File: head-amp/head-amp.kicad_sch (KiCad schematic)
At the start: 32 parts, among them IC1 OPA1642AID

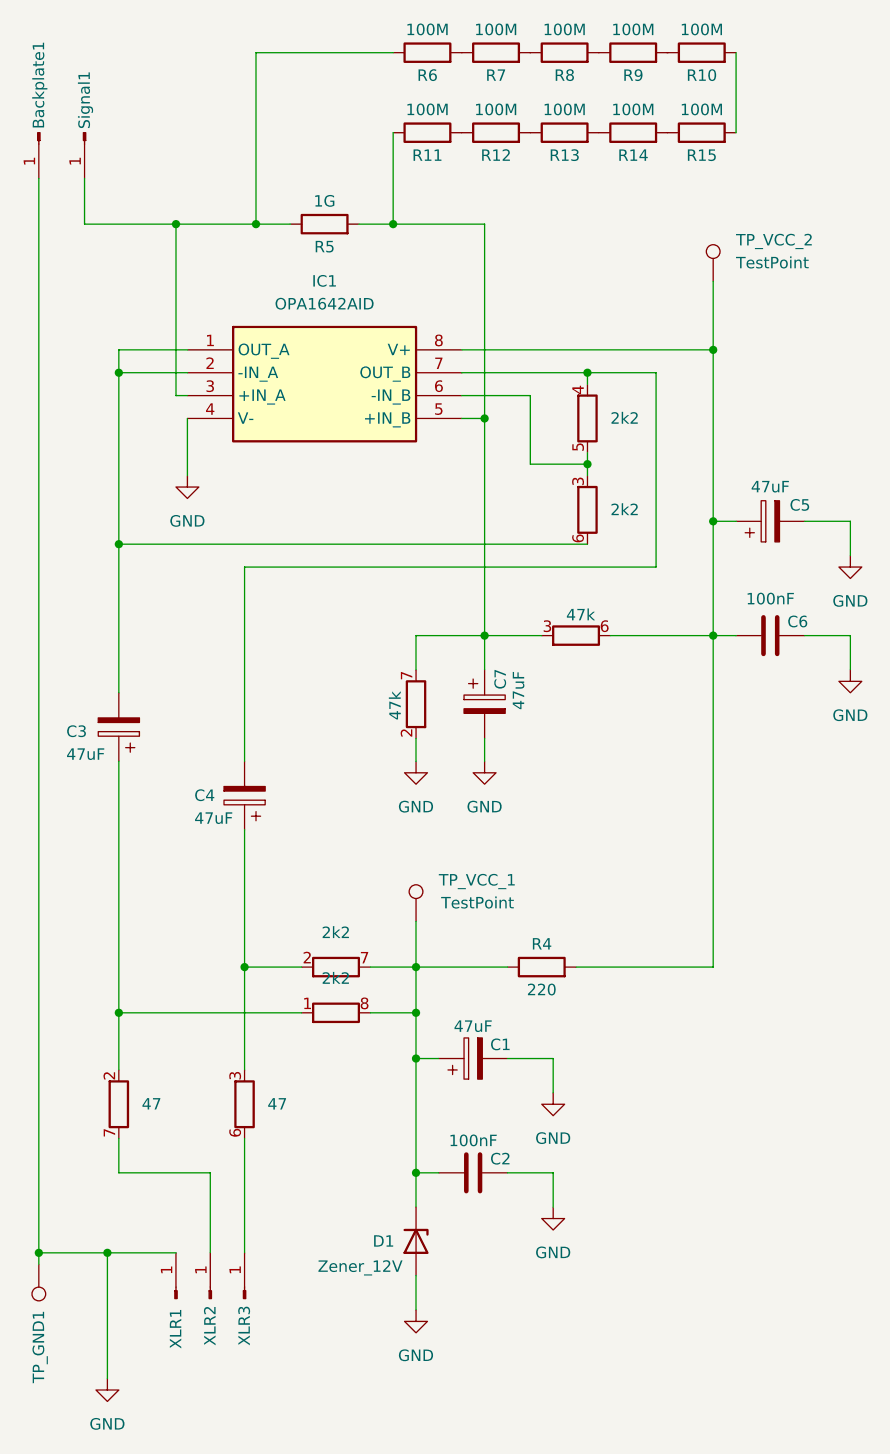
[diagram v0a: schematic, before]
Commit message: Finished head amp PCB layout, generated gerber + BOM
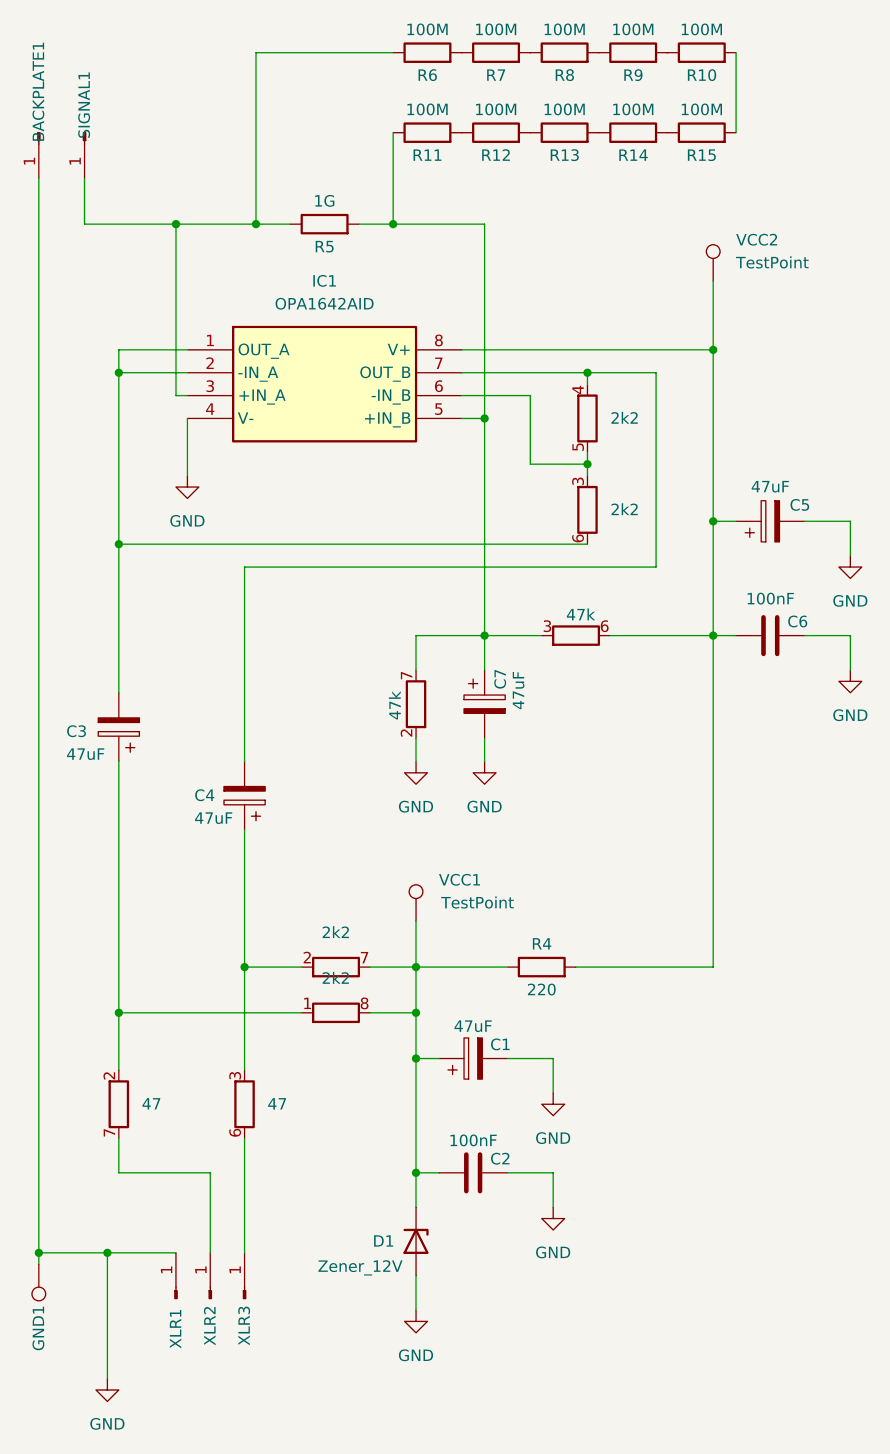
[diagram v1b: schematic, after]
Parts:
- BACKPLATE1: renamed from Backplate1; footprint Connector_Wire:SolderWire-0.1sqmm_1x01_D0.4mm_OD1mm -> Connector_Wire:SolderWire-0.25sqmm_1x01_D0.65mm_OD2mm
- SIGNAL1: renamed from Signal1; footprint Connector_Wire:SolderWire-0.1sqmm_1x01_D0.4mm_OD1mm -> Connector_Wire:SolderWire-0.25sqmm_1x01_D0.65mm_OD2mm
- XLR1, XLR2, XLR3: footprint Connector_Wire:SolderWire-0.1sqmm_1x01_D0.4mm_OD1mm -> Connector_Wire:SolderWire-0.25sqmm_1x01_D0.65mm_OD2mm
- renumbered TP_GND1 to GND1, TP_VCC_1 to VCC1, TP_VCC_2 to VCC2
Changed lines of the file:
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@@
 		(on_board yes)
 		(dnp no)
-		(property "Reference" "TP_GND1"
-			(at 43.18 178.308 90)
+		(property "Reference" "GND1"
+			(at 43.18 174.752 90)
 			(effects
 				(font
@@
 			(project "head-amp"
 				(path "/7025f093-8497-445c-bb21-7e3d97d178d1"
-					(reference "TP_GND1")
+					(reference "GND1")
 					(unit 1)
 				)
@@
 			)
 		)
-		(property "Footprint" "Connector_Wire:SolderWire-0.1sqmm_1x01_D0.4mm_OD1mm"
+		(property "Footprint" "Connector_Wire:SolderWire-0.25sqmm_1x01_D0.65mm_OD2mm"
 			(at 62.23 168.91 0)
 			(effects
@@
 		(on_board yes)
 		(dnp no)
-		(property "Reference" "Signal1"
+		(property "Reference" "SIGNAL1"
 			(at 48.26 32.512 0)
 			(effects
@@
 			)
 		)
-		(property "Footprint" "Connector_Wire:SolderWire-0.1sqmm_1x01_D0.4mm_OD1mm"
+		(property "Footprint" "Connector_Wire:SolderWire-0.25sqmm_1x01_D0.65mm_OD2mm"
 			(at 48.26 39.37 0)
 			(effects
@@
 			(project "head-amp"
 				(path "/7025f093-8497-445c-bb21-7e3d97d178d1"
-					(reference "Signal1")
+					(reference "SIGNAL1")
 					(unit 1)
 				)
@@
 		(dnp no)
 		(fields_autoplaced yes)
-		(property "Reference" "TP_VCC_2"
+		(property "Reference" "VCC2"
 			(at 120.65 51.3079 0)
 			(effects
@@
 			(project ""
 				(path "/7025f093-8497-445c-bb21-7e3d97d178d1"
-					(reference "TP_VCC_2")
+					(reference "VCC2")
 					(unit 1)
 				)
@@
 		(on_board yes)
 		(dnp no)
-		(property "Reference" "Backplate1"
+		(property "Reference" "BACKPLATE1"
 			(at 43.18 29.21 0)
 			(effects
@@
 			)
 		)
-		(property "Footprint" "Connector_Wire:SolderWire-0.1sqmm_1x01_D0.4mm_OD1mm"
+		(property "Footprint" "Connector_Wire:SolderWire-0.25sqmm_1x01_D0.65mm_OD2mm"
 			(at 43.18 39.37 0)
 			(effects
@@
 			)
 		)
-		(property "Datasheet" "~"
+		(property "Datasheet" ""
 			(at 43.18 39.37 0)
 			(effects
@@
 			(project ""
 				(path "/7025f093-8497-445c-bb21-7e3d97d178d1"
-					(reference "Backplate1")
+					(reference "BACKPLATE1")
 					(unit 1)
 				)
@@
 			)
 		)
-		(property "Footprint" "Connector_Wire:SolderWire-0.1sqmm_1x01_D0.4mm_OD1mm"
+		(property "Footprint" "Connector_Wire:SolderWire-0.25sqmm_1x01_D0.65mm_OD2mm"
 			(at 66.04 168.91 0)
 			(effects
@@
 		(on_board yes)
 		(dnp no)
-		(property "Reference" "TP_VCC_1"
+		(property "Reference" "VCC1"
 			(at 87.63 122.4279 0)
 			(effects
@@
 			(project "head-amp"
 				(path "/7025f093-8497-445c-bb21-7e3d97d178d1"
-					(reference "TP_VCC_1")
+					(reference "VCC1")
 					(unit 1)
 				)
@@
 			)
 		)
-		(property "Footprint" "Connector_Wire:SolderWire-0.1sqmm_1x01_D0.4mm_OD1mm"
+		(property "Footprint" "Connector_Wire:SolderWire-0.25sqmm_1x01_D0.65mm_OD2mm"
 			(at 58.42 168.91 0)
 			(effects

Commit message: input/output connectors moved to 2.54mm spacing. Improved clearance around screw slots.
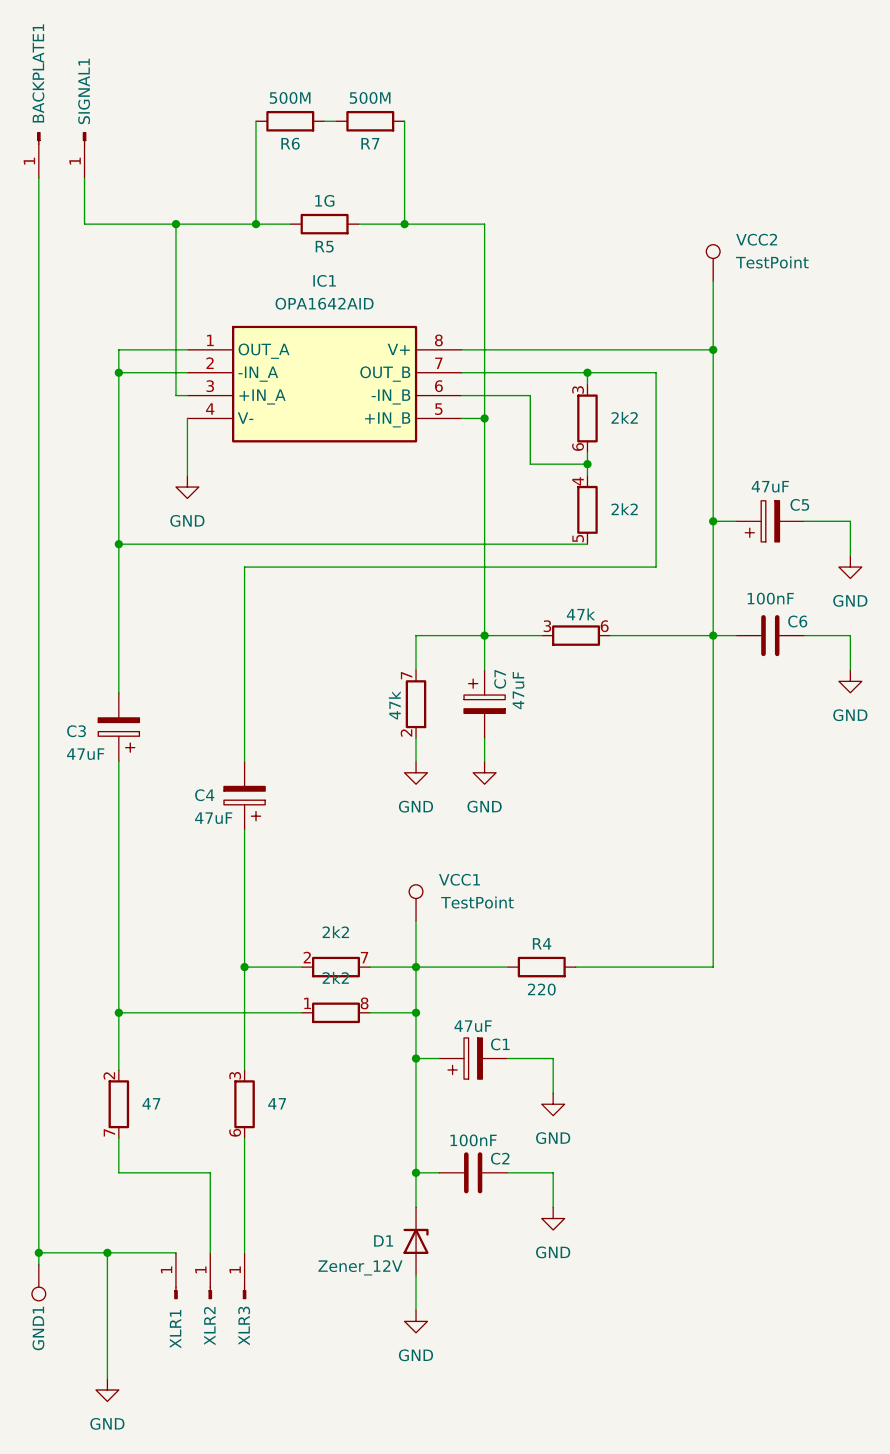
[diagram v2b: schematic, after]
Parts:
- removed R10, R12, R13, R14, R15, R7, R8, R9: 100M, Resistor_SMD:R_0805_2012Metric, symbol Device:R
- D1: footprint Diode_SMD:D_SOD-323 -> Diode_SMD:D_SOD-123
- IC1: footprint SOIC127P600X175-8N -> OPA1642_VSSOP-8:DGK8
- R5: footprint 01_Custom:R_Axial_THT-SMD-Dual -> Resistor_THT:R_Axial_DIN0207_L6.3mm_D2.5mm_P10.16mm_Horizontal
- R6: value 100M -> 500M; footprint Resistor_SMD:R_0805_2012Metric -> Resistor_SMD:R_1206_3216Metric
- R7: renamed from R11; value 100M -> 500M; footprint Resistor_SMD:R_0805_2012Metric -> Resistor_SMD:R_1206_3216Metric
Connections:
- net at C7.1, IC1.5 (+IN_B), R3.3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: now also R7.2; no longer R7.1
- net at R6.2: now also R7.1
- net at C3.2, IC1.1 (OUT_A), IC1.2 (-IN_A): now also R2.5; no longer R2.6
- net at C4.2, IC1.7 (OUT_B): now also R2.3; no longer R2.4
- new net: IC1.6 (-IN_B), R2.4, R2.6
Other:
- moved on the sheet: R6, R7
